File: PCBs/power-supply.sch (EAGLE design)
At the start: 46 parts, among them U3 TL783

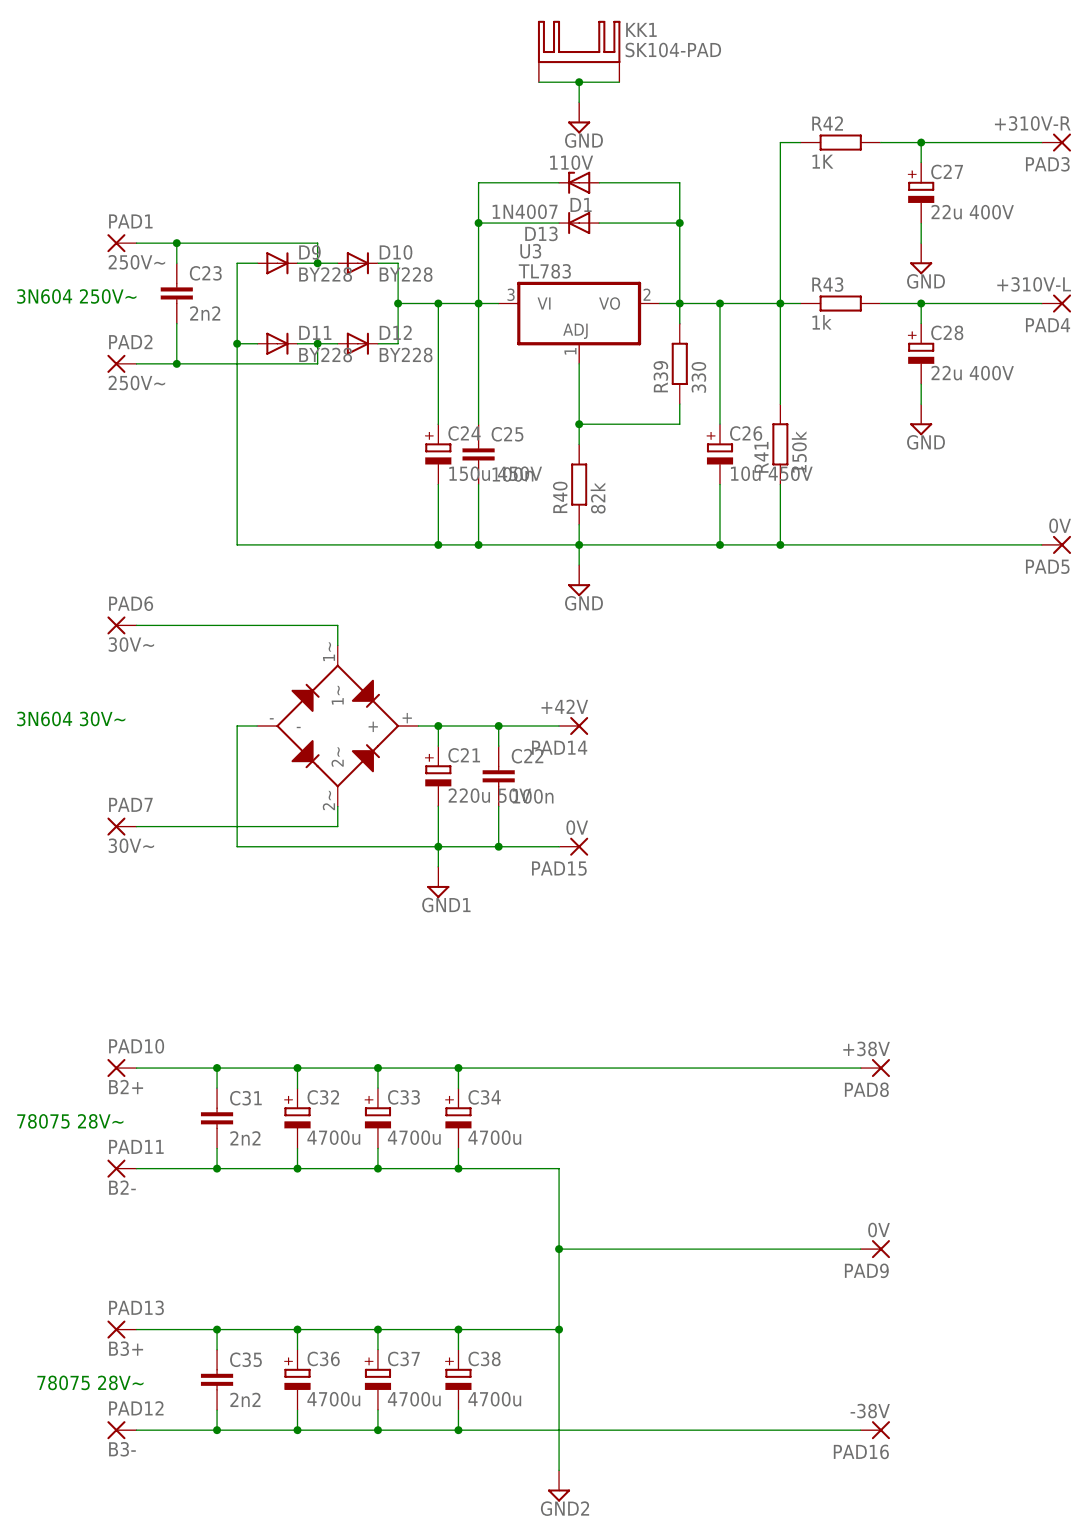
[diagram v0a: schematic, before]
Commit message: Started amp.
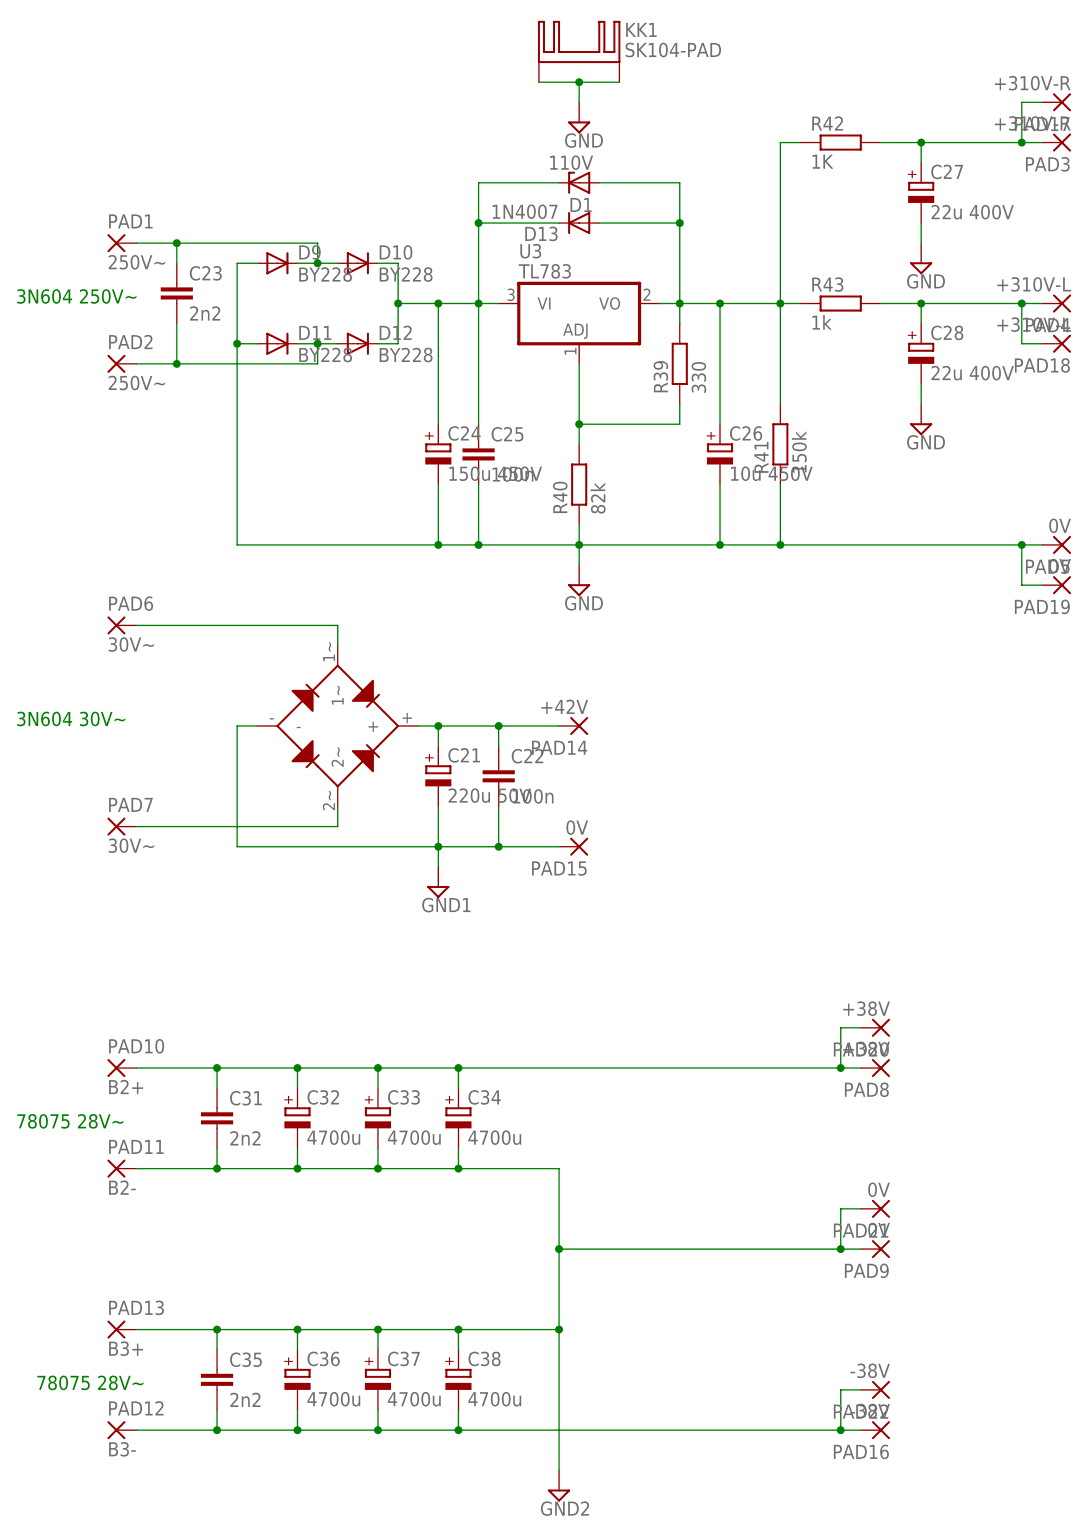
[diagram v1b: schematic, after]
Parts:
- added PAD17: +310V-R, wirepad:WIREPAD3,81/1,4
- added PAD18: +310V-L, wirepad:WIREPAD3,81/1,4
- added PAD19, PAD21: 0V, wirepad:WIREPAD3,81/1,4
- added PAD20: +38V, wirepad:WIREPAD3,81/1,4
- added PAD22: -38V, wirepad:WIREPAD3,81/1,4
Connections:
- net GND: now also PAD19.P
- net GND2: now also PAD21.P
- net N$10: now also PAD20.P
- net N$13: now also PAD22.P
- net N$3: now also PAD17.P
- net N$7: now also PAD18.P
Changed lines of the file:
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@@
 <part name="PAD9" library="wirepad" library_urn="urn:adsk.eagle:library:412" deviceset="WIREPAD" device="3,81/1,4" package3d_urn="urn:adsk.eagle:package:30835/1" value="0V"/>
 <part name="PAD16" library="wirepad" library_urn="urn:adsk.eagle:library:412" deviceset="WIREPAD" device="3,81/1,4" package3d_urn="urn:adsk.eagle:package:30835/1" value="-38V"/>
+<part name="PAD17" library="wirepad" library_urn="urn:adsk.eagle:library:412" deviceset="WIREPAD" device="3,81/1,4" package3d_urn="urn:adsk.eagle:package:30835/1" value="+310V-R"/>
+<part name="PAD18" library="wirepad" library_urn="urn:adsk.eagle:library:412" deviceset="WIREPAD" device="3,81/1,4" package3d_urn="urn:adsk.eagle:package:30835/1" value="+310V-L"/>
+<part name="PAD19" library="wirepad" library_urn="urn:adsk.eagle:library:412" deviceset="WIREPAD" device="3,81/1,4" package3d_urn="urn:adsk.eagle:package:30835/1" value="0V"/>
+<part name="PAD20" library="wirepad" library_urn="urn:adsk.eagle:library:412" deviceset="WIREPAD" device="3,81/1,4" package3d_urn="urn:adsk.eagle:package:30835/1" value="+38V"/>
+<part name="PAD21" library="wirepad" library_urn="urn:adsk.eagle:library:412" deviceset="WIREPAD" device="3,81/1,4" package3d_urn="urn:adsk.eagle:package:30835/1" value="0V"/>
+<part name="PAD22" library="wirepad" library_urn="urn:adsk.eagle:library:412" deviceset="WIREPAD" device="3,81/1,4" package3d_urn="urn:adsk.eagle:package:30835/1" value="-38V"/>
 </parts>
 <sheets>
@@
 <instance part="PAD9" gate="G$1" x="106.68" y="-38.1" rot="R180"/>
 <instance part="PAD16" gate="G$1" x="106.68" y="-60.96" rot="R180"/>
+<instance part="PAD17" gate="G$1" x="129.54" y="106.68" rot="R180"/>
+<instance part="PAD18" gate="G$1" x="129.54" y="76.2" rot="R180"/>
+<instance part="PAD19" gate="G$1" x="129.54" y="45.72" rot="R180"/>
+<instance part="PAD20" gate="G$1" x="106.68" y="-10.16" rot="R180"/>
+<instance part="PAD21" gate="G$1" x="106.68" y="-33.02" rot="R180"/>
+<instance part="PAD22" gate="G$1" x="106.68" y="-55.88" rot="R180"/>
 </instances>
 <busses>
@@
 <wire x1="106.68" y1="101.6" x2="111.76" y2="101.6" width="0.1524" layer="91"/>
 <pinref part="C27" gate="G$1" pin="+"/>
-<wire x1="111.76" y1="101.6" x2="127" y2="101.6" width="0.1524" layer="91"/>
+<wire x1="111.76" y1="101.6" x2="124.46" y2="101.6" width="0.1524" layer="91"/>
+<wire x1="124.46" y1="101.6" x2="127" y2="101.6" width="0.1524" layer="91"/>
 <wire x1="111.76" y1="99.06" x2="111.76" y2="101.6" width="0.1524" layer="91"/>
 <junction x="111.76" y="101.6"/>
 <pinref part="PAD3" gate="G$1" pin="P"/>
+<pinref part="PAD17" gate="G$1" pin="P"/>
+<wire x1="127" y1="106.68" x2="124.46" y2="106.68" width="0.1524" layer="91"/>
+<wire x1="124.46" y1="106.68" x2="124.46" y2="101.6" width="0.1524" layer="91"/>
+<junction x="124.46" y="101.6"/>
 </segment>
 </net>
@@
 <wire x1="106.68" y1="81.28" x2="111.76" y2="81.28" width="0.1524" layer="91"/>
 <pinref part="C28" gate="G$1" pin="+"/>
-<wire x1="111.76" y1="81.28" x2="127" y2="81.28" width="0.1524" layer="91"/>
+<wire x1="111.76" y1="81.28" x2="124.46" y2="81.28" width="0.1524" layer="91"/>
+<wire x1="124.46" y1="81.28" x2="127" y2="81.28" width="0.1524" layer="91"/>
 <wire x1="111.76" y1="78.74" x2="111.76" y2="81.28" width="0.1524" layer="91"/>
 <junction x="111.76" y="81.28"/>
 <pinref part="PAD4" gate="G$1" pin="P"/>
+<pinref part="PAD18" gate="G$1" pin="P"/>
+<wire x1="127" y1="76.2" x2="124.46" y2="76.2" width="0.1524" layer="91"/>
+<wire x1="124.46" y1="76.2" x2="124.46" y2="81.28" width="0.1524" layer="91"/>
+<junction x="124.46" y="81.28"/>
 </segment>
 </net>
@@
 <wire x1="33.02" y1="-15.24" x2="43.18" y2="-15.24" width="0.1524" layer="91"/>
 <wire x1="43.18" y1="-15.24" x2="53.34" y2="-15.24" width="0.1524" layer="91"/>
-<wire x1="53.34" y1="-15.24" x2="104.14" y2="-15.24" width="0.1524" layer="91"/>
+<wire x1="53.34" y1="-15.24" x2="101.6" y2="-15.24" width="0.1524" layer="91"/>
+<wire x1="101.6" y1="-15.24" x2="104.14" y2="-15.24" width="0.1524" layer="91"/>
 <wire x1="22.86" y1="-17.78" x2="22.86" y2="-15.24" width="0.1524" layer="91"/>
 <junction x="22.86" y="-15.24"/>
@@
 <junction x="53.34" y="-15.24"/>
 <pinref part="PAD8" gate="G$1" pin="P"/>
+<pinref part="PAD20" gate="G$1" pin="P"/>
+<wire x1="104.14" y1="-10.16" x2="101.6" y2="-10.16" width="0.1524" layer="91"/>
+<wire x1="101.6" y1="-10.16" x2="101.6" y2="-15.24" width="0.1524" layer="91"/>
+<junction x="101.6" y="-15.24"/>
 </segment>
 </net>
@@
 <wire x1="33.02" y1="-60.96" x2="43.18" y2="-60.96" width="0.1524" layer="91"/>
 <wire x1="43.18" y1="-60.96" x2="53.34" y2="-60.96" width="0.1524" layer="91"/>
-<wire x1="53.34" y1="-60.96" x2="104.14" y2="-60.96" width="0.1524" layer="91"/>
+<wire x1="53.34" y1="-60.96" x2="101.6" y2="-60.96" width="0.1524" layer="91"/>
+<wire x1="101.6" y1="-60.96" x2="104.14" y2="-60.96" width="0.1524" layer="91"/>
 <wire x1="22.86" y1="-58.42" x2="22.86" y2="-60.96" width="0.1524" layer="91"/>
 <junction x="22.86" y="-60.96"/>
@@
 <junction x="53.34" y="-60.96"/>
 <pinref part="PAD16" gate="G$1" pin="P"/>
+<pinref part="PAD22" gate="G$1" pin="P"/>
+<wire x1="104.14" y1="-55.88" x2="101.6" y2="-55.88" width="0.1524" layer="91"/>
+<wire x1="101.6" y1="-55.88" x2="101.6" y2="-60.96" width="0.1524" layer="91"/>
+<junction x="101.6" y="-60.96"/>
 </segment>
 </net>
@@
 <pinref part="D11" gate="1" pin="A"/>
 <wire x1="86.36" y1="50.8" x2="93.98" y2="50.8" width="0.1524" layer="91"/>
-<wire x1="93.98" y1="50.8" x2="127" y2="50.8" width="0.1524" layer="91"/>
+<wire x1="93.98" y1="50.8" x2="124.46" y2="50.8" width="0.1524" layer="91"/>
+<wire x1="124.46" y1="50.8" x2="127" y2="50.8" width="0.1524" layer="91"/>
 <wire x1="27.94" y1="76.2" x2="25.4" y2="76.2" width="0.1524" layer="91"/>
 <wire x1="25.4" y1="76.2" x2="25.4" y2="86.36" width="0.1524" layer="91"/>
@@
 <junction x="50.8" y="50.8"/>
 <pinref part="SUPPLY3" gate="GND" pin="GND"/>
+<pinref part="PAD19" gate="G$1" pin="P"/>
+<wire x1="127" y1="45.72" x2="124.46" y2="45.72" width="0.1524" layer="91"/>
+<wire x1="124.46" y1="45.72" x2="124.46" y2="50.8" width="0.1524" layer="91"/>
+<junction x="124.46" y="50.8"/>
 </segment>
 <segment>
@@
 <wire x1="66.04" y1="-38.1" x2="66.04" y2="-27.94" width="0.1524" layer="91"/>
 <wire x1="66.04" y1="-66.04" x2="66.04" y2="-48.26" width="0.1524" layer="91"/>
-<wire x1="66.04" y1="-38.1" x2="104.14" y2="-38.1" width="0.1524" layer="91"/>
+<wire x1="66.04" y1="-38.1" x2="101.6" y2="-38.1" width="0.1524" layer="91"/>
 <pinref part="PAD9" gate="G$1" pin="P"/>
 <junction x="66.04" y="-38.1"/>
-</segment>
-</net>
+<pinref part="PAD21" gate="G$1" pin="P"/>
+<wire x1="101.6" y1="-38.1" x2="104.14" y2="-38.1" width="0.1524" layer="91"/>
+<wire x1="104.14" y1="-33.02" x2="101.6" y2="-33.02" width="0.1524" layer="91"/>
+<wire x1="101.6" y1="-33.02" x2="101.6" y2="-38.1" width="0.1524" layer="91"/>
+<junction x="101.6" y="-38.1"/>
+</segment>
+</net>

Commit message: Basic design done.
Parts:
- added PAD23: +42V, wirepad:WIREPAD3,81/1,4
- added PAD24: 0V, wirepad:WIREPAD3,81/1,4
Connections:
- net GND1: now also PAD24.P
- net N$15: now also PAD23.P
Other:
- moved on the sheet: PAD17, PAD18, PAD19, PAD20, PAD21, PAD22
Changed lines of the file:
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@@
 <part name="PAD21" library="wirepad" library_urn="urn:adsk.eagle:library:412" deviceset="WIREPAD" device="3,81/1,4" package3d_urn="urn:adsk.eagle:package:30835/1" value="0V"/>
 <part name="PAD22" library="wirepad" library_urn="urn:adsk.eagle:library:412" deviceset="WIREPAD" device="3,81/1,4" package3d_urn="urn:adsk.eagle:package:30835/1" value="-38V"/>
+<part name="PAD23" library="wirepad" library_urn="urn:adsk.eagle:library:412" deviceset="WIREPAD" device="3,81/1,4" package3d_urn="urn:adsk.eagle:package:30835/1" value="+42V"/>
+<part name="PAD24" library="wirepad" library_urn="urn:adsk.eagle:library:412" deviceset="WIREPAD" device="3,81/1,4" package3d_urn="urn:adsk.eagle:package:30835/1" value="0V"/>
 </parts>
 <sheets>
@@
 <instance part="PAD9" gate="G$1" x="106.68" y="-38.1" rot="R180"/>
 <instance part="PAD16" gate="G$1" x="106.68" y="-60.96" rot="R180"/>
-<instance part="PAD17" gate="G$1" x="129.54" y="106.68" rot="R180"/>
-<instance part="PAD18" gate="G$1" x="129.54" y="76.2" rot="R180"/>
-<instance part="PAD19" gate="G$1" x="129.54" y="45.72" rot="R180"/>
-<instance part="PAD20" gate="G$1" x="106.68" y="-10.16" rot="R180"/>
-<instance part="PAD21" gate="G$1" x="106.68" y="-33.02" rot="R180"/>
-<instance part="PAD22" gate="G$1" x="106.68" y="-55.88" rot="R180"/>
+<instance part="PAD17" gate="G$1" x="129.54" y="109.22" rot="R180"/>
+<instance part="PAD18" gate="G$1" x="129.54" y="73.66" rot="R180"/>
+<instance part="PAD19" gate="G$1" x="129.54" y="43.18" rot="R180"/>
+<instance part="PAD20" gate="G$1" x="106.68" y="-7.62" rot="R180"/>
+<instance part="PAD21" gate="G$1" x="106.68" y="-30.48" rot="R180"/>
+<instance part="PAD22" gate="G$1" x="106.68" y="-53.34" rot="R180"/>
+<instance part="PAD23" gate="G$1" x="68.58" y="35.56" rot="R180"/>
+<instance part="PAD24" gate="G$1" x="68.58" y="5.08" rot="R180"/>
 </instances>
 <busses>
@@
 <pinref part="PAD3" gate="G$1" pin="P"/>
 <pinref part="PAD17" gate="G$1" pin="P"/>
-<wire x1="127" y1="106.68" x2="124.46" y2="106.68" width="0.1524" layer="91"/>
-<wire x1="124.46" y1="106.68" x2="124.46" y2="101.6" width="0.1524" layer="91"/>
+<wire x1="127" y1="109.22" x2="124.46" y2="109.22" width="0.1524" layer="91"/>
+<wire x1="124.46" y1="109.22" x2="124.46" y2="101.6" width="0.1524" layer="91"/>
 <junction x="124.46" y="101.6"/>
 </segment>
@@
 <pinref part="PAD4" gate="G$1" pin="P"/>
 <pinref part="PAD18" gate="G$1" pin="P"/>
-<wire x1="127" y1="76.2" x2="124.46" y2="76.2" width="0.1524" layer="91"/>
-<wire x1="124.46" y1="76.2" x2="124.46" y2="81.28" width="0.1524" layer="91"/>
+<wire x1="127" y1="73.66" x2="124.46" y2="73.66" width="0.1524" layer="91"/>
+<wire x1="124.46" y1="73.66" x2="124.46" y2="81.28" width="0.1524" layer="91"/>
 <junction x="124.46" y="81.28"/>
 </segment>
@@
 <pinref part="C21" gate="G$1" pin="+"/>
 <wire x1="50.8" y1="27.94" x2="58.42" y2="27.94" width="0.1524" layer="91"/>
-<wire x1="58.42" y1="27.94" x2="66.04" y2="27.94" width="0.1524" layer="91"/>
+<wire x1="58.42" y1="27.94" x2="63.5" y2="27.94" width="0.1524" layer="91"/>
+<wire x1="63.5" y1="27.94" x2="66.04" y2="27.94" width="0.1524" layer="91"/>
 <wire x1="50.8" y1="25.4" x2="50.8" y2="27.94" width="0.1524" layer="91"/>
 <junction x="50.8" y="27.94"/>
@@
 <junction x="58.42" y="27.94"/>
 <pinref part="PAD14" gate="G$1" pin="P"/>
+<pinref part="PAD23" gate="G$1" pin="P"/>
+<wire x1="66.04" y1="35.56" x2="63.5" y2="35.56" width="0.1524" layer="91"/>
+<wire x1="63.5" y1="35.56" x2="63.5" y2="27.94" width="0.1524" layer="91"/>
+<junction x="63.5" y="27.94"/>
 </segment>
 </net>
@@
 <pinref part="PAD8" gate="G$1" pin="P"/>
 <pinref part="PAD20" gate="G$1" pin="P"/>
-<wire x1="104.14" y1="-10.16" x2="101.6" y2="-10.16" width="0.1524" layer="91"/>
-<wire x1="101.6" y1="-10.16" x2="101.6" y2="-15.24" width="0.1524" layer="91"/>
+<wire x1="104.14" y1="-7.62" x2="101.6" y2="-7.62" width="0.1524" layer="91"/>
+<wire x1="101.6" y1="-7.62" x2="101.6" y2="-15.24" width="0.1524" layer="91"/>
 <junction x="101.6" y="-15.24"/>
 </segment>
@@
 <pinref part="PAD16" gate="G$1" pin="P"/>
 <pinref part="PAD22" gate="G$1" pin="P"/>
-<wire x1="104.14" y1="-55.88" x2="101.6" y2="-55.88" width="0.1524" layer="91"/>
-<wire x1="101.6" y1="-55.88" x2="101.6" y2="-60.96" width="0.1524" layer="91"/>
+<wire x1="104.14" y1="-53.34" x2="101.6" y2="-53.34" width="0.1524" layer="91"/>
+<wire x1="101.6" y1="-53.34" x2="101.6" y2="-60.96" width="0.1524" layer="91"/>
 <junction x="101.6" y="-60.96"/>
 </segment>
@@
 <pinref part="SUPPLY3" gate="GND" pin="GND"/>
 <pinref part="PAD19" gate="G$1" pin="P"/>
-<wire x1="127" y1="45.72" x2="124.46" y2="45.72" width="0.1524" layer="91"/>
-<wire x1="124.46" y1="45.72" x2="124.46" y2="50.8" width="0.1524" layer="91"/>
+<wire x1="127" y1="43.18" x2="124.46" y2="43.18" width="0.1524" layer="91"/>
+<wire x1="124.46" y1="43.18" x2="124.46" y2="50.8" width="0.1524" layer="91"/>
 <junction x="124.46" y="50.8"/>
 </segment>
@@
 <pinref part="C22" gate="G$1" pin="2"/>
 <wire x1="50.8" y1="12.7" x2="58.42" y2="12.7" width="0.1524" layer="91"/>
-<wire x1="58.42" y1="12.7" x2="66.04" y2="12.7" width="0.1524" layer="91"/>
+<wire x1="58.42" y1="12.7" x2="63.5" y2="12.7" width="0.1524" layer="91"/>
+<wire x1="63.5" y1="12.7" x2="66.04" y2="12.7" width="0.1524" layer="91"/>
 <wire x1="58.42" y1="17.78" x2="58.42" y2="12.7" width="0.1524" layer="91"/>
 <junction x="58.42" y="12.7"/>
@@
 <pinref part="SUPPLY1" gate="G$1" pin="GND1"/>
 <wire x1="50.8" y1="10.16" x2="50.8" y2="12.7" width="0.1524" layer="91"/>
+<pinref part="PAD24" gate="G$1" pin="P"/>
+<wire x1="66.04" y1="5.08" x2="63.5" y2="5.08" width="0.1524" layer="91"/>
+<wire x1="63.5" y1="5.08" x2="63.5" y2="12.7" width="0.1524" layer="91"/>
+<junction x="63.5" y="12.7"/>
 </segment>
 </net>
@@
 <pinref part="PAD21" gate="G$1" pin="P"/>
 <wire x1="101.6" y1="-38.1" x2="104.14" y2="-38.1" width="0.1524" layer="91"/>
-<wire x1="104.14" y1="-33.02" x2="101.6" y2="-33.02" width="0.1524" layer="91"/>
-<wire x1="101.6" y1="-33.02" x2="101.6" y2="-38.1" width="0.1524" layer="91"/>
+<wire x1="104.14" y1="-30.48" x2="101.6" y2="-30.48" width="0.1524" layer="91"/>
+<wire x1="101.6" y1="-30.48" x2="101.6" y2="-38.1" width="0.1524" layer="91"/>
 <junction x="101.6" y="-38.1"/>
 </segment>
